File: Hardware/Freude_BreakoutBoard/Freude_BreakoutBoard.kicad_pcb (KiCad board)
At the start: 4 copper layers, 21.2 x 36 mm, 11 parts, among them J10 Conn_01x06_Female, J11 Conn_01x05_Male, J12 Conn_01x05_Female, J5 Conn_01x06_Female, J6 Conn_01x06_Male, J7 Conn_01x03_Female, J8 Conn_01x06_Male, J9 Conn_01x06_Female, U3 TLV713185PDBV

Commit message: remove inner layers
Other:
- copper layers 4 -> 2

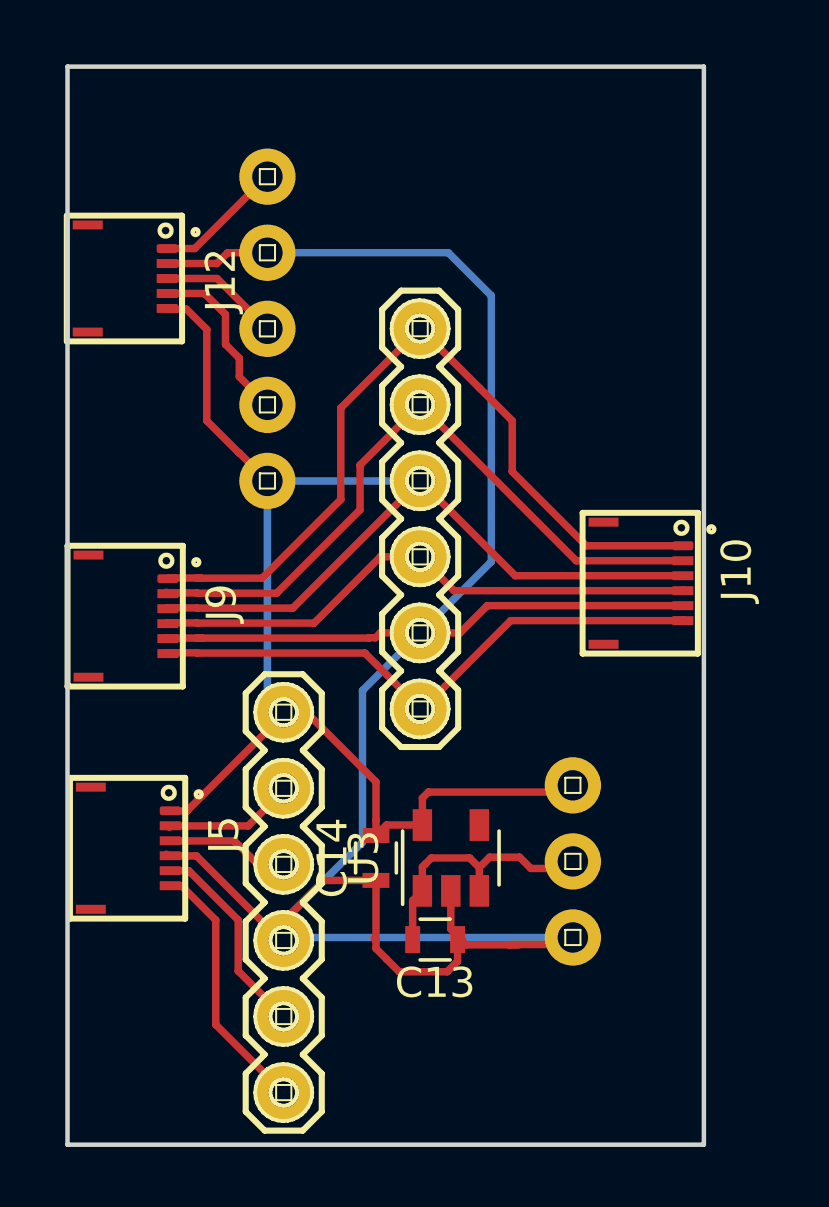
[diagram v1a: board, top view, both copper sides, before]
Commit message: add silk to breakout :|
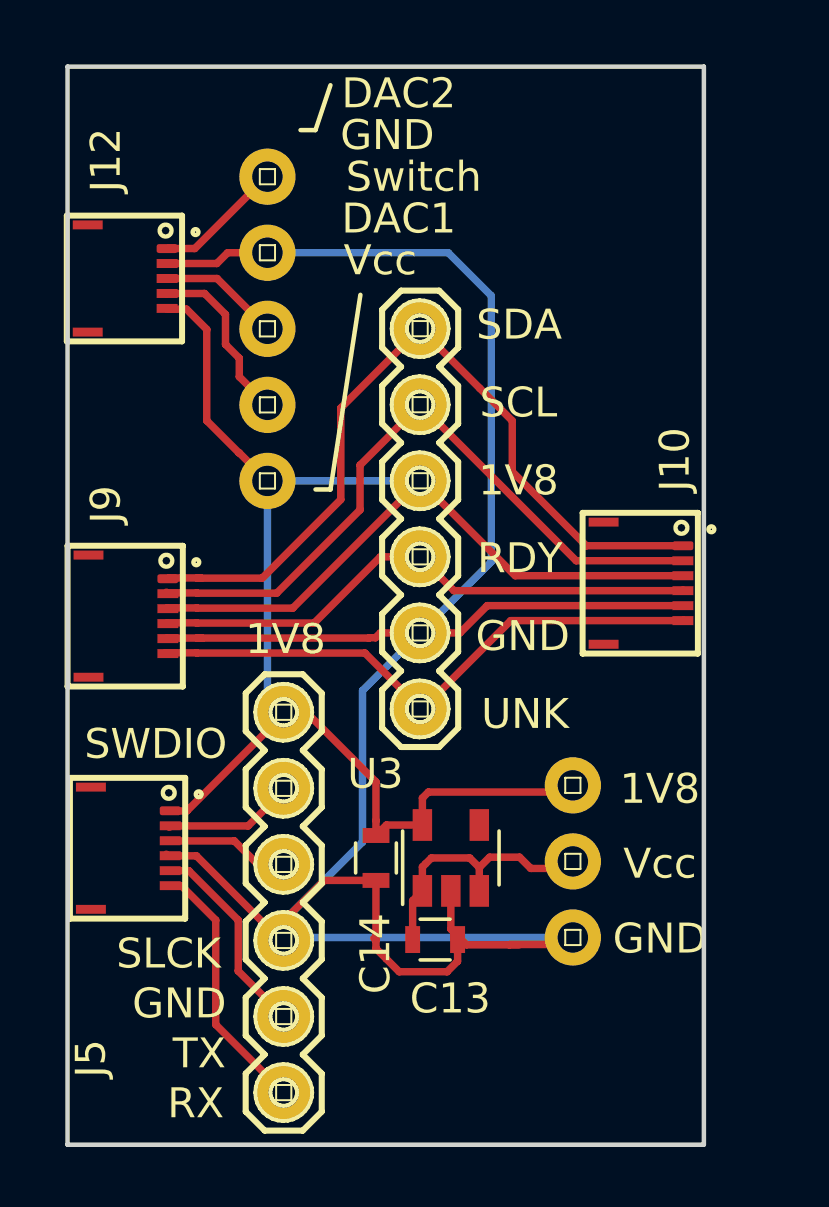
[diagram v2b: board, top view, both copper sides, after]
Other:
- board text added: "1V8"
- board text added: "DAC1"
- board text added: "DAC2"
- board text added: "GND"
- board text added: "RDY"
- board text added: "RX"
- board text added: "SCL"
- board text added: "SDA"
- board text added: "SLCK"
- board text added: "SWDIO"
- board text added: "Switch"
- board text added: "TX"
- board text added: "UNK"
- board text added: "Vcc"

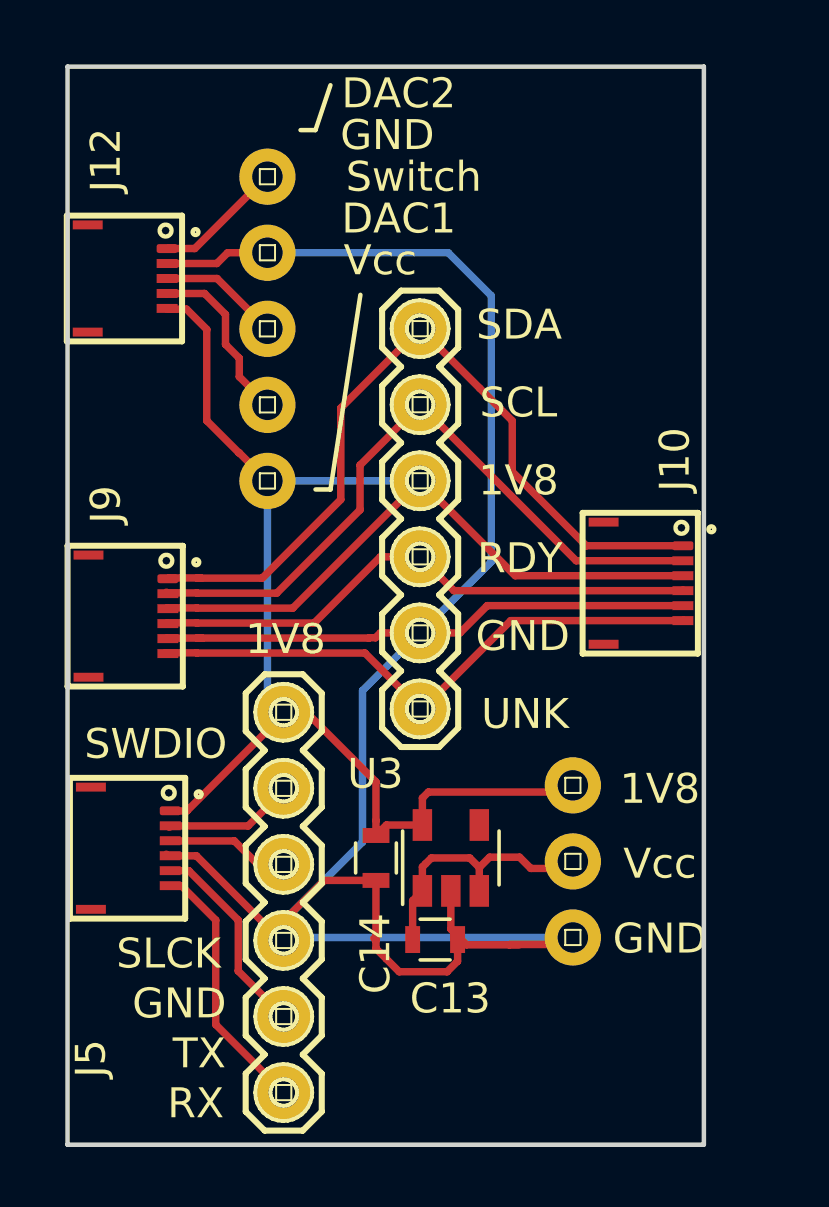
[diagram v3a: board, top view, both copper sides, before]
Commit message: resolves 10, resolves 9, resolves 6, resolves 5, add ground ring around touch sensor, add ground ring on top, separate RX from TX and include ground plane between
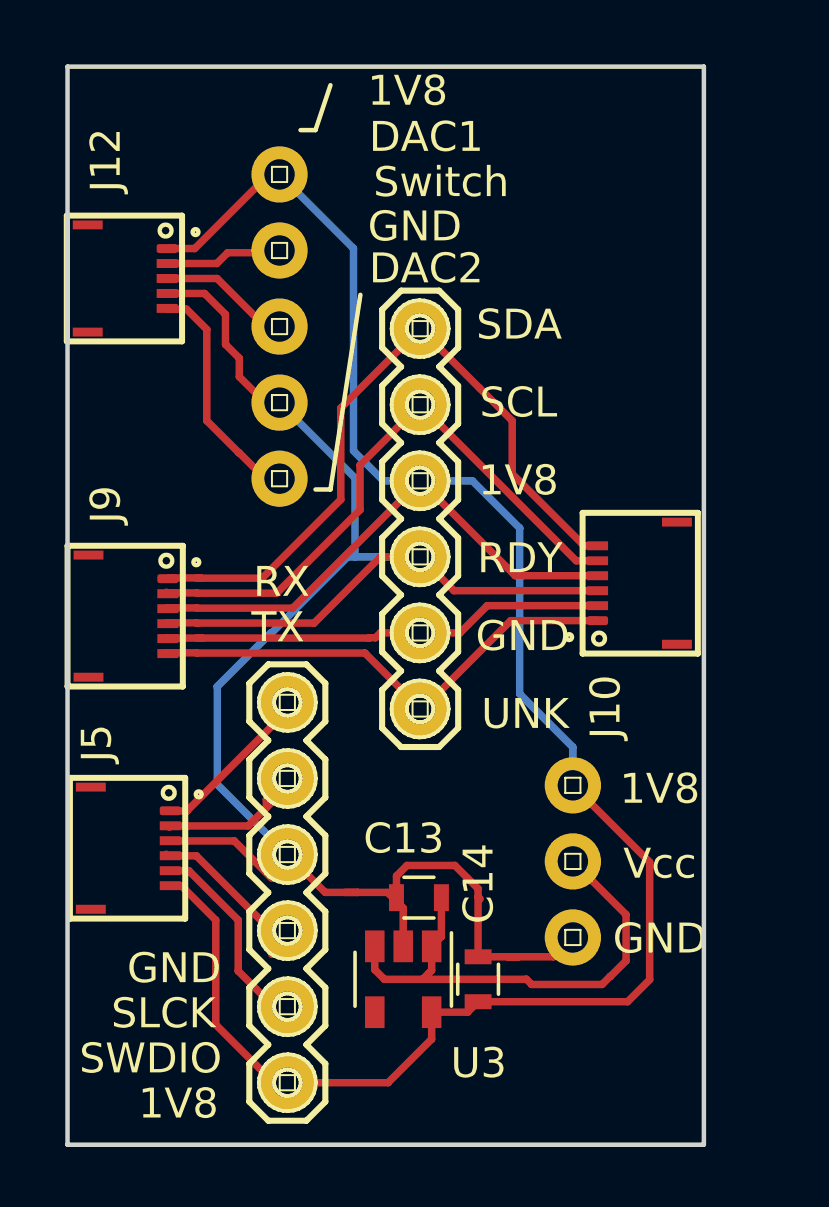
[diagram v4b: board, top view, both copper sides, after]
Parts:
- moved J6 12.4 mm to (155.6, 97.3), turned to 90 degrees
- moved J11 10.1 mm to (155.3, 77.1), turned to 90 degrees
- moved C14 5.29 mm to (161.9, 93.9), turned to 270 degrees
- moved U3 4.35 mm to (159.4, 93.9), turned to 270 degrees
- moved J10 2.85 mm to (165.9, 80.6), turned to 90 degrees
- moved C13 1.50 mm to (160.0, 91.1), turned to 0 degrees
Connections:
- J10 pad 1: /SDA_BO -> /UNK_BO
- J10 pad 2: /SCL_BO -> /RDY_BO
- J10 pad 3: +1V8 -> GND
- J10 pad 4: /RDY_BO -> +1V8
- J10 pad 5: GND -> /SCL_BO
- J10 pad 6: /UNK_BO -> /SDA_BO
- J12 pad 1: /DAC2_OUT1_BO -> +1V8
- J12 pad 2: GND -> /DAC1_OUT2_BO
- J12 pad 4: /DAC1_OUT2_BO -> GND
- J12 pad 5: +1V8 -> /DAC2_OUT1_BO
- J5 pad 1: +1V8 -> /Prog_RX
- J5 pad 2: /Prog_SWDIO -> /Prog_TX
- J5 pad 3: /Prog_SWCLK -> GND
- J5 pad 4: GND -> /Prog_SWCLK
- J5 pad 5: /Prog_TX -> /Prog_SWDIO
- J5 pad 6: /Prog_RX -> +1V8
- J8 pad 4: /RDY_BO -> GND
- J8 pad 5: GND -> /RDY_BO
- J9 pad 4: /RDY_BO -> GND
- J9 pad 5: GND -> /RDY_BO
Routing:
- net GND: track 86.8 -> 64.4 mm
- net +1V8: track 59.3 -> 79.4 mm
- net VCC: track 8.84 -> 16.7 mm
- net /RDY_BO: track 18.9 -> 15.8 mm
- net /Prog_SWDIO: track 3.77 -> 6.80 mm
- net /SCL_BO: track 23.0 -> 20.1 mm
- net /UNK_BO: track 19.4 -> 16.5 mm
- net /Prog_RX: track 8.70 -> 5.88 mm
- net /SDA_BO: track 26.6 -> 23.8 mm
- net /DAC2_OUT1_BO: track 4.91 -> 7.49 mm
- net /DAC1_OUT2_BO: track 5.88 -> 3.48 mm
- net /Prog_TX: track 6.80 -> 5.03 mm
- net /Prog_SWCLK: track 3.99 -> 5.37 mm
